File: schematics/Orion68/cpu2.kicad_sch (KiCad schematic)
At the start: 39 parts, among them J10 Conn_02x08_Counter_Clockwise, J600 Euro96pin, J601 clock, J602 clock1, Q7 2N3904, Q8 2N3904, SW3 Reset, U16 74LS139, U2.? ICM7555xB, U21 74LS20, U22 74HC164, U24 74HC4078, U600 68000D, U601 74LS393, U602 74HC74, U603 74HC14, U604 ATmega8-16P

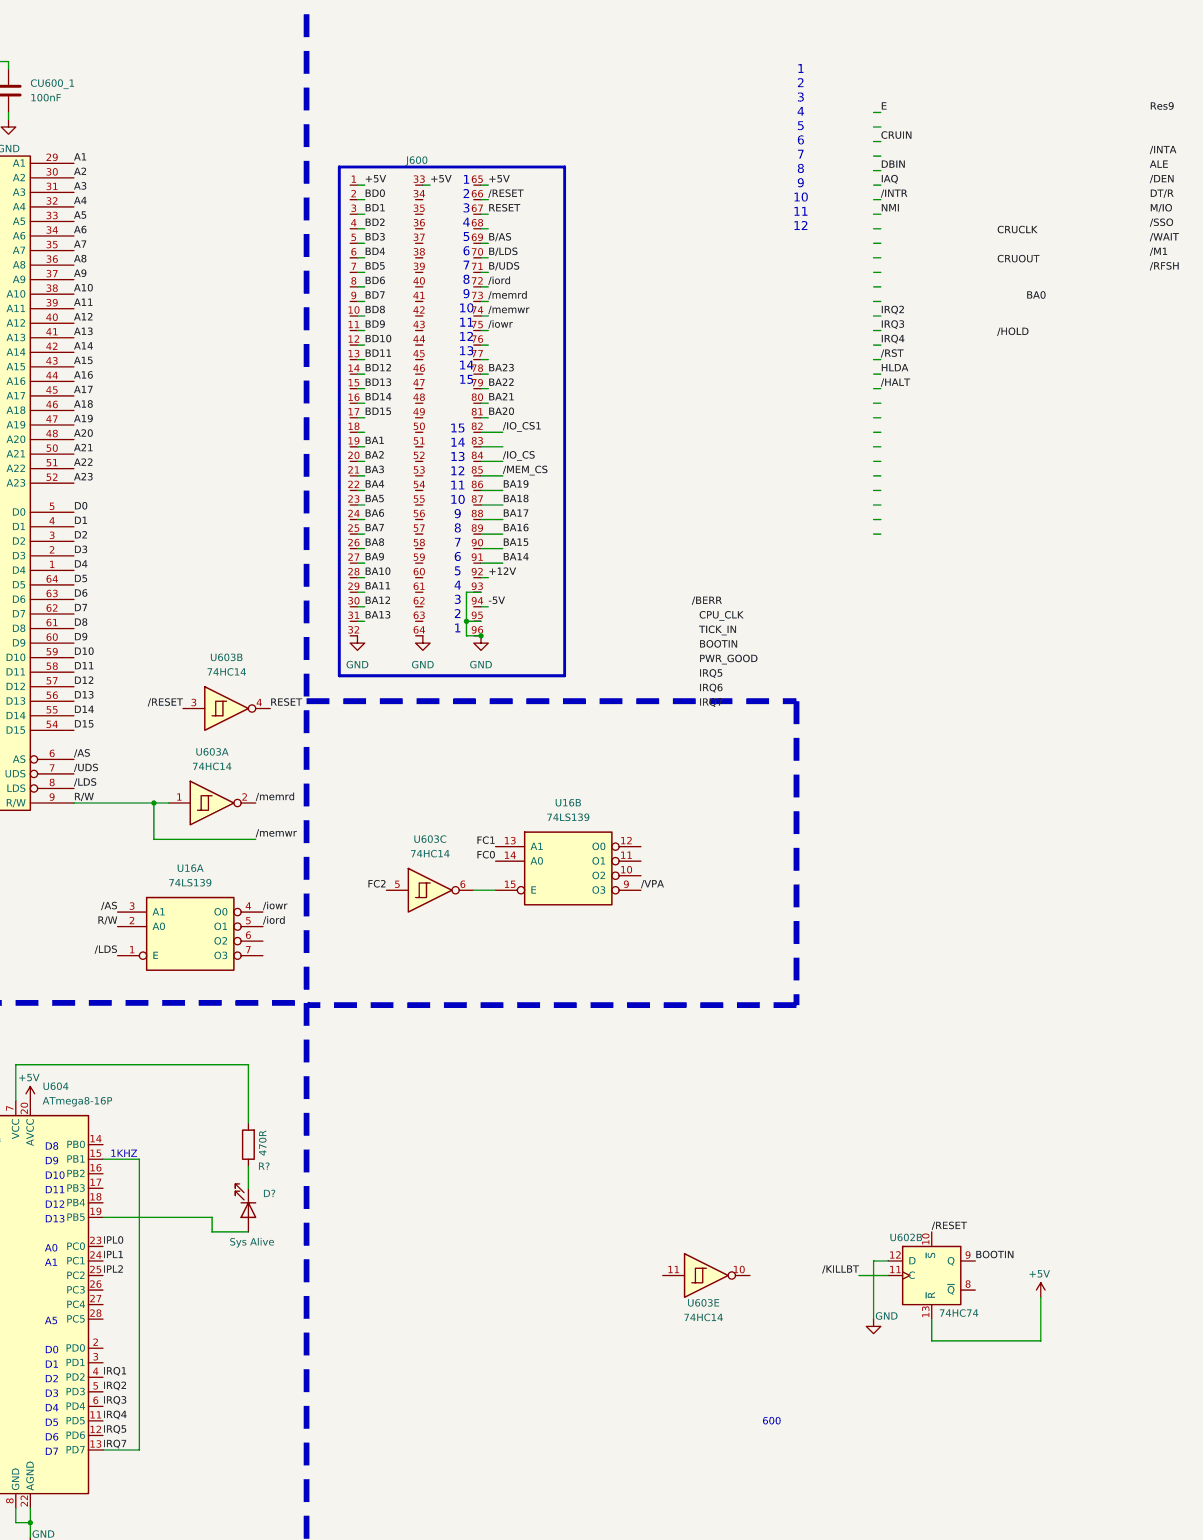
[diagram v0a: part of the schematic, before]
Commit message: Added drv_keboard
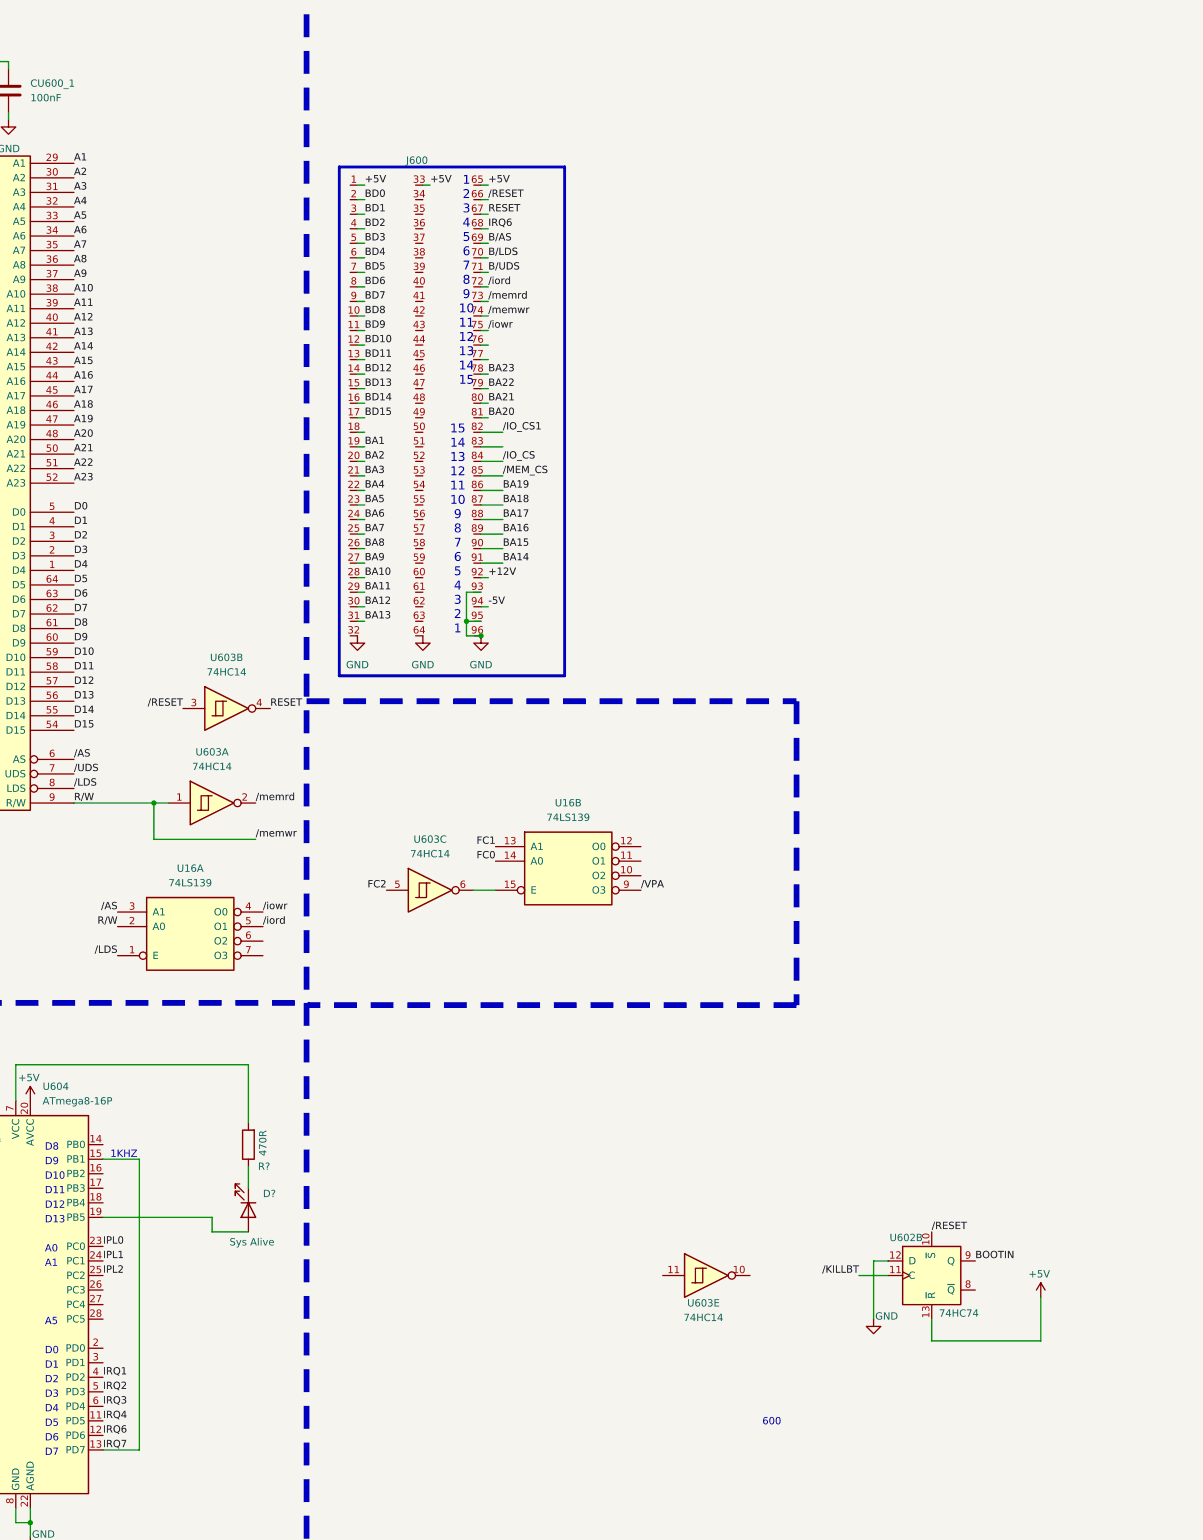
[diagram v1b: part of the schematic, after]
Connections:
- net IRQ5 is gone; now on net IRQ6: U604.12 (PD6)
- net IRQ6: now also J600.68
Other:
- note removed: "1 2 3 4 5 6 7 8 9 10 11 12"

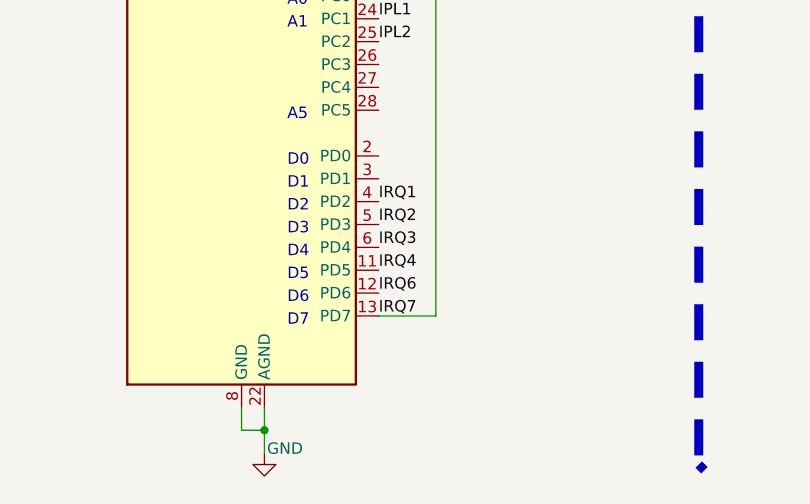
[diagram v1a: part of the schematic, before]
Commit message: Implemented interrupted 2 for systick
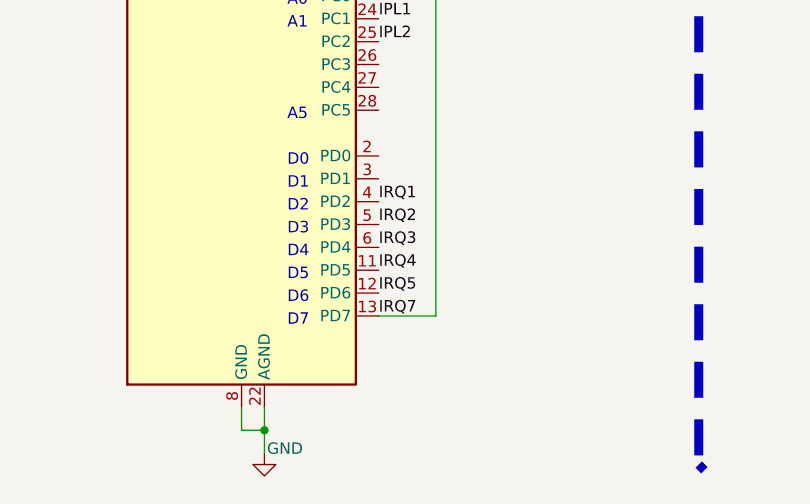
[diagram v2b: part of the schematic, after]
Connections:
- net IRQ6: no longer U604.12 (PD6)
- new net IRQ5: U604.12 (PD6)
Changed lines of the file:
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@@
 		)
 	)
-	(label "IRQ6"
+	(label "IRQ5"
 		(at 233.68 259.08 0)
 		(effects

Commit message: Implementation drive ide initiated
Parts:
- added J6: systemTickFreq, symbol Connector_Generic:Conn_02x03_Counter_Clockwise
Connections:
- net GND: now also J6.4 (Pin_4), J6.5 (Pin_5), J6.6 (Pin_6)
- net at U604.26 (PC3): now also J6.1 (Pin_1)
- net at U604.27 (PC4): now also J6.2 (Pin_2)
- net at U604.28 (PC5): now also J6.3 (Pin_3)
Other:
- note added: "1-6 - 10ms 2-5 - 5ms 3-4 - 1ms"
- note added: "FALTA IMPLEMENTAR"
- note added: "livre"
